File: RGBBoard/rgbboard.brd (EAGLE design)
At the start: 70 x 70 mm, 33 parts, among them J1 BOOT, J2 5.5x2.1mm Barrel, U1 MIC5219 5V, U2 ATMEGA328P_TQFP, U3 V_REG_317SMD, Y1 16MHz

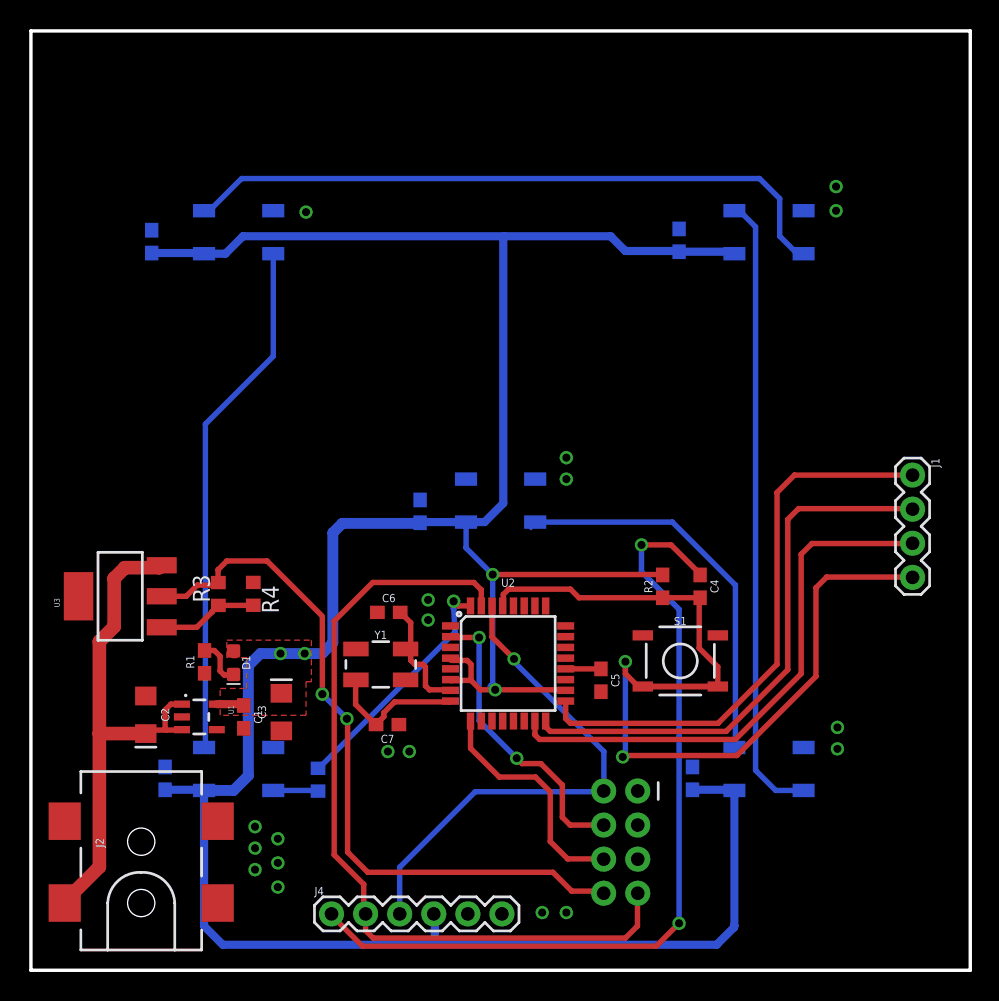
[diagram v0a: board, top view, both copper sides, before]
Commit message: Layout Done - Need to Pass DRC
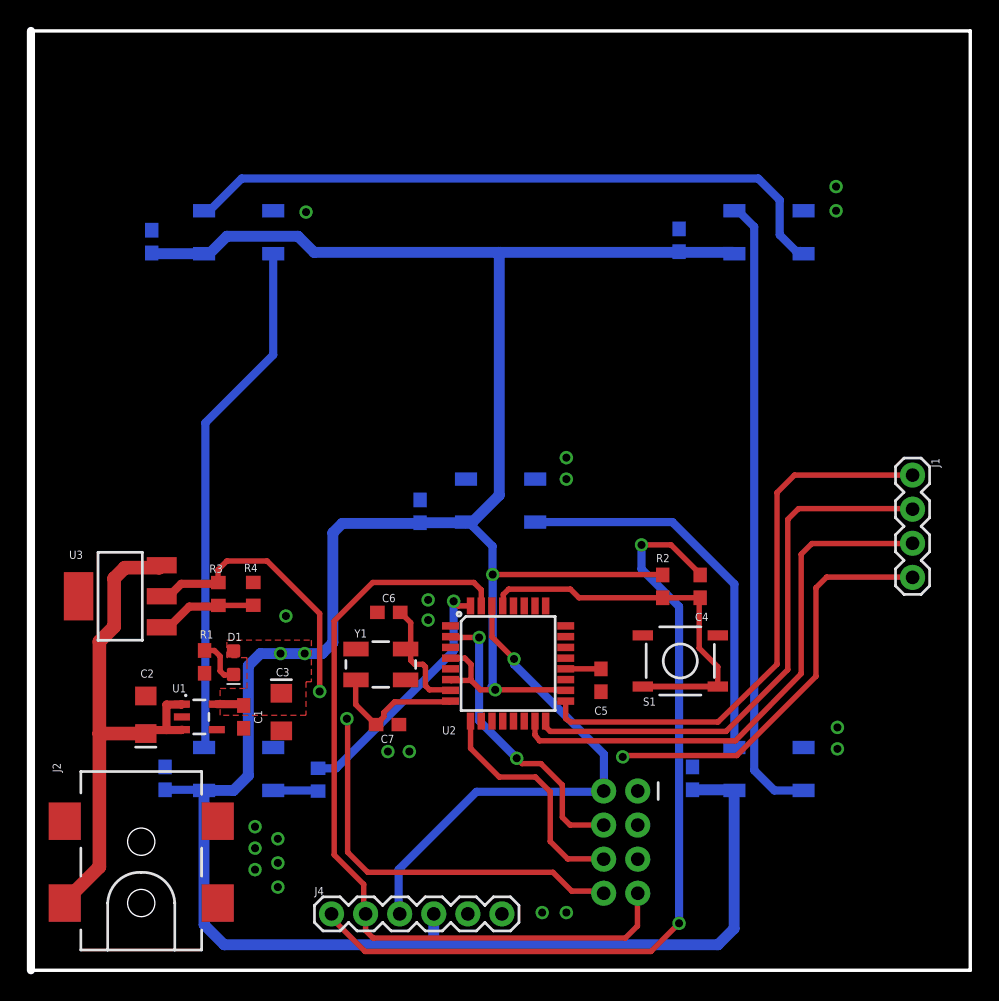
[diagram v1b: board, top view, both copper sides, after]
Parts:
- J3: value (none) -> ESP
- J4: value (none) -> PROG
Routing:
- net RESET: track 75.0 -> 65.6 mm, vias 2 -> 1
- net 3.3V: track 53.9 -> 51.3 mm
- net 5V: track 214.8 -> 212.5 mm
- net N$5: track 29.7 -> 28.9 mm
- net RX: track 38.7 -> 38.0 mm
- net DIN: track 18.2 -> 18.9 mm
